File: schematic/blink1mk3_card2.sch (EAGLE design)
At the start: 39 parts, among them J1 NONPOP, U1 EFM32HG309F64G, X1 USBPCB2SIDE, X2 USBPCB2

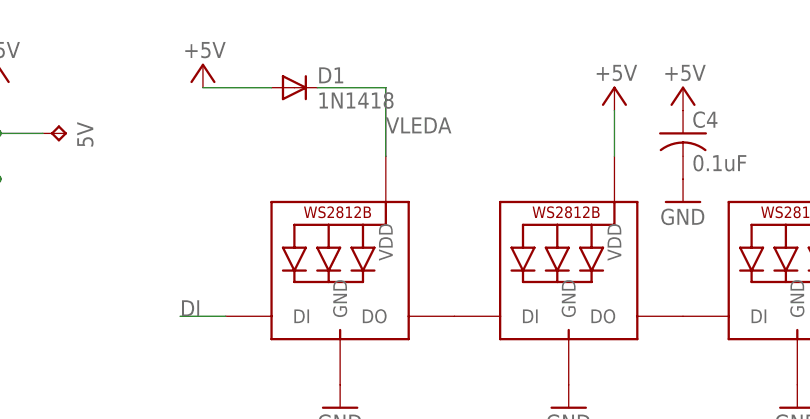
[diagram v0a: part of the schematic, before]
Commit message: small blink1mk3_card2 pcb fixes
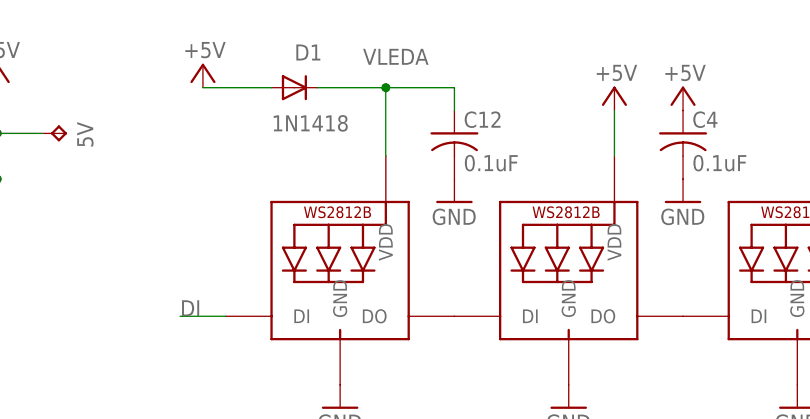
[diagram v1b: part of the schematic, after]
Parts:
- added C12: 0.1uF, adafruit:C-USC0603
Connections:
- net GND: now also C12.2
- net VLEDA: now also C12.1
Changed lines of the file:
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@@
 <part name="GND7" library="supply1" library_urn="urn:adsk.eagle:library:371" deviceset="GND" device=""/>
 <part name="X1" library="todstuff" library_urn="urn:adsk.eagle:library:1731349" deviceset="USB" device="PCB2SIDE" package3d_urn="urn:adsk.eagle:package:3133264/1"/>
+<part name="C12" library="adafruit" library_urn="urn:adsk.eagle:library:420" deviceset="C-US" device="C0603" value="0.1uF"/>
+<part name="GND24" library="supply1" library_urn="urn:adsk.eagle:library:371" deviceset="GND" device=""/>
 </parts>
 <sheets>
@@
 <instance part="D" gate="G$1" x="27.94" y="127" rot="R90"/>
 <instance part="C" gate="G$1" x="27.94" y="129.54" rot="R90"/>
-<instance part="D1" gate="G$1" x="182.88" y="175.26"/>
+<instance part="D1" gate="G$1" x="182.88" y="175.26" smashed="yes">
+<attribute name="NAME" x="182.88" y="178.2826" size="1.778" layer="95"/>
+<attribute name="VALUE" x="180.34" y="170.4086" size="1.778" layer="96"/>
+</instance>
 <instance part="C4" gate="G$1" x="226.06" y="170.18"/>
 <instance part="LED1" gate="G$1" x="187.96" y="152.4"/>
@@
 <instance part="GND7" gate="1" x="106.68" y="40.64"/>
 <instance part="X1" gate="G$1" x="121.92" y="22.86"/>
+<instance part="C12" gate="G$1" x="200.66" y="170.18"/>
+<instance part="GND24" gate="1" x="200.66" y="162.56"/>
 </instances>
 <busses>
@@
 <pinref part="U$2" gate="G$1" pin="C"/>
 <pinref part="GND7" gate="1" pin="GND"/>
+</segment>
+<segment>
+<pinref part="C12" gate="G$1" pin="2"/>
+<pinref part="GND24" gate="1" pin="GND"/>
 </segment>
 </net>
@@
 <segment>
 <wire x1="193.04" y1="175.26" x2="193.04" y2="167.64" width="0.1524" layer="91"/>
-<label x="193.04" y="170.18" size="1.778" layer="95"/>
+<label x="190.5" y="177.8" size="1.778" layer="95"/>
 <wire x1="185.42" y1="175.26" x2="193.04" y2="175.26" width="0.1524" layer="91"/>
 <pinref part="D1" gate="G$1" pin="C"/>
 <pinref part="LED1" gate="G$1" pin="VDD"/>
-</segment>
-</net>
+<pinref part="C12" gate="G$1" pin="1"/>
+<wire x1="193.04" y1="175.26" x2="200.66" y2="175.26" width="0.1524" layer="91"/>
+<wire x1="200.66" y1="175.26" x2="200.66" y2="172.72" width="0.1524" layer="91"/>
+<junction x="193.04" y="175.26"/>
+</segment>
+</net>
